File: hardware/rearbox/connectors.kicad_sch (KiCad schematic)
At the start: 2 parts, among them J3 Conn_02x28_Top_Bottom, J4 Auxiliary

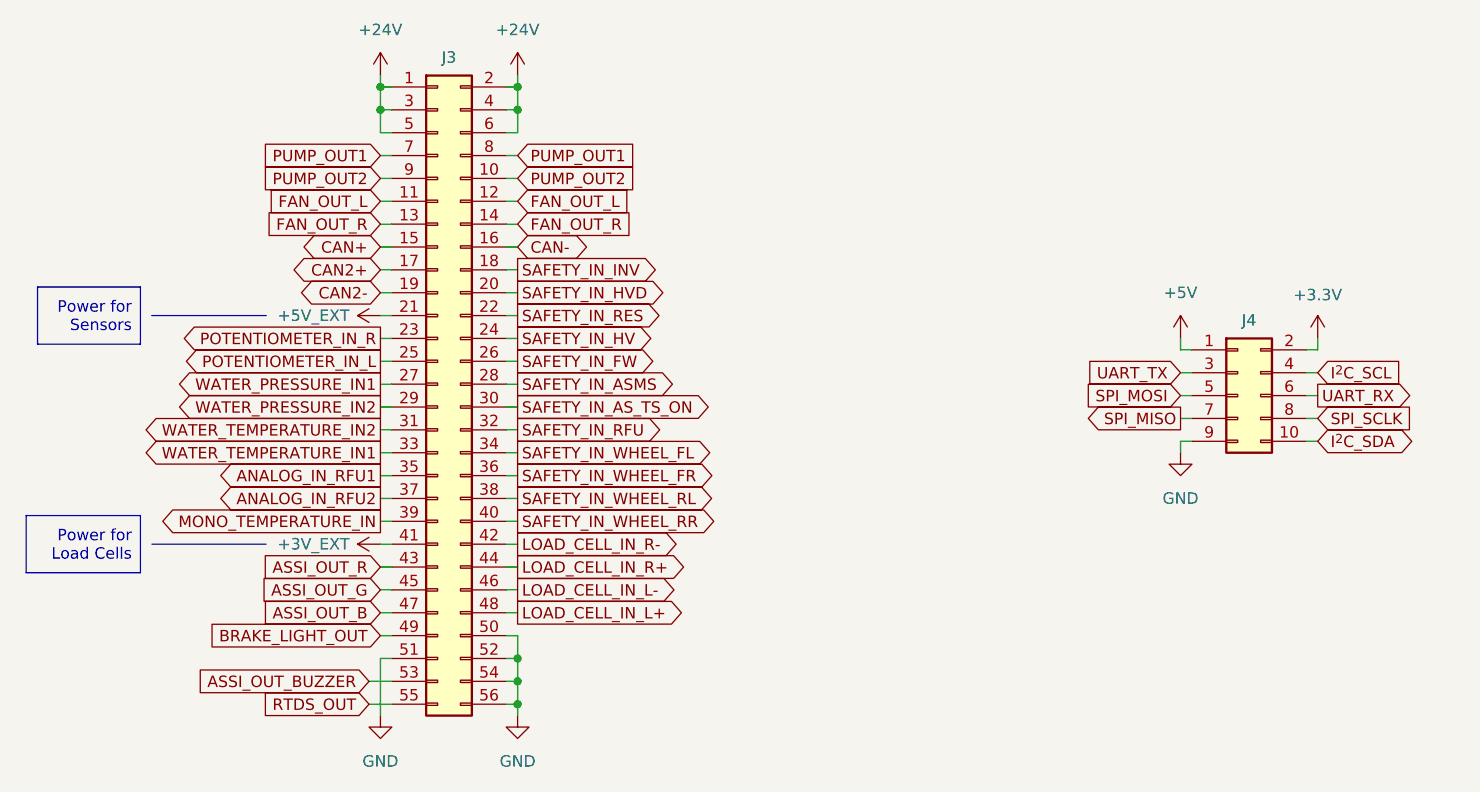
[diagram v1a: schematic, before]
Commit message: Deleted measurement systems for new iteration
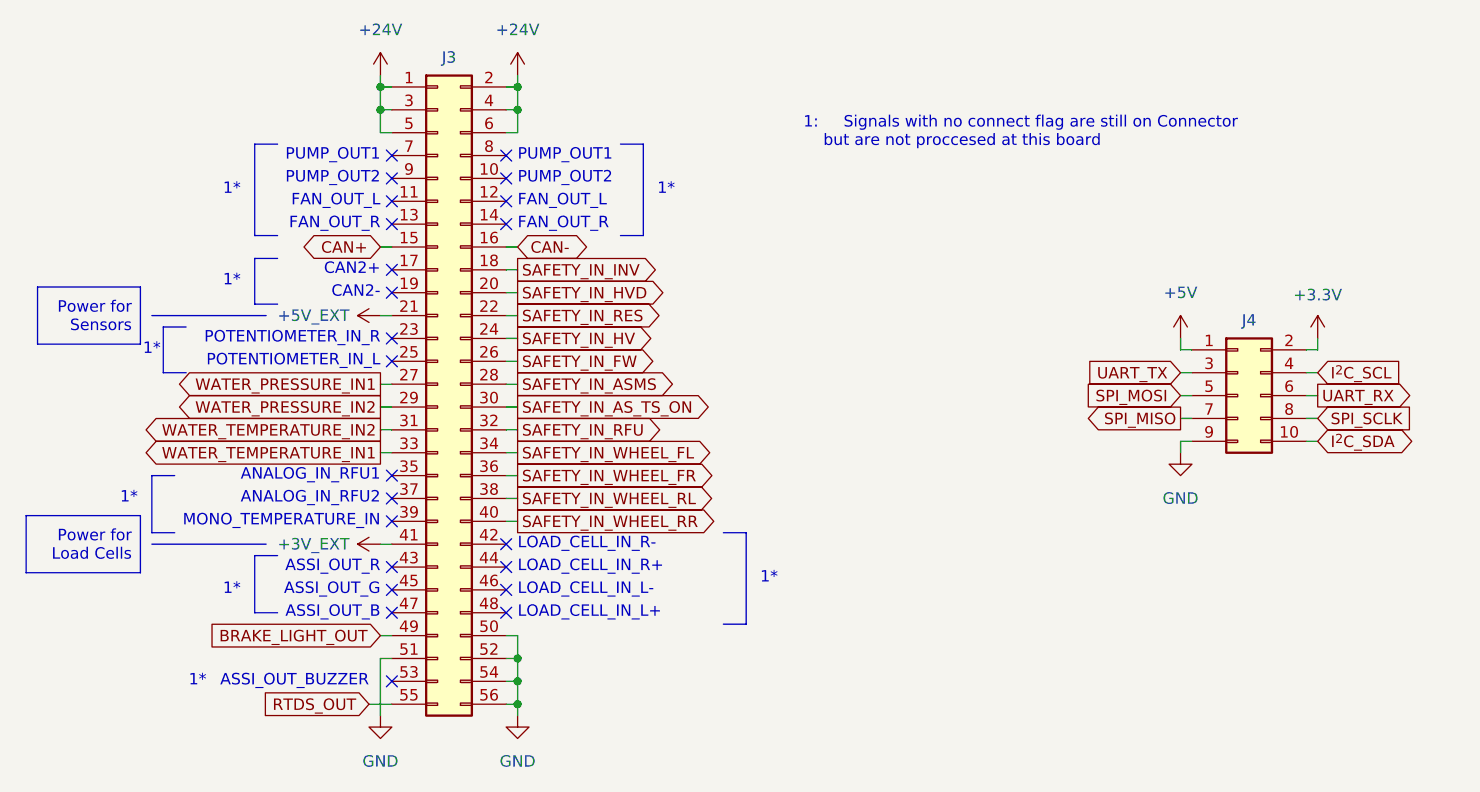
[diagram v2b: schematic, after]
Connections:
- net ANALOG_IN_RFU1: no longer names the net of J3.35 (Pin_35)
- net ANALOG_IN_RFU2: no longer names the net of J3.37 (Pin_37)
- net ASSI_OUT_B: no longer names the net of J3.47 (Pin_47)
- net ASSI_OUT_BUZZER: no longer names the net of J3.53 (Pin_53)
- net ASSI_OUT_G: no longer names the net of J3.45 (Pin_45)
- net ASSI_OUT_R: no longer names the net of J3.43 (Pin_43)
- net CAN2+: no longer names the net of J3.17 (Pin_17)
- net CAN2-: no longer names the net of J3.19 (Pin_19)
- net FAN_OUT_L: no longer names the net of J3.11 (Pin_11)
- net FAN_OUT_L: no longer J3.12 (Pin_12)
- net FAN_OUT_R: no longer names the net of J3.13 (Pin_13)
- net FAN_OUT_R: no longer J3.14 (Pin_14)
- net LOAD_CELL_IN_L+: no longer names the net of J3.48 (Pin_48)
- net LOAD_CELL_IN_L-: no longer names the net of J3.46 (Pin_46)
- net LOAD_CELL_IN_R+: no longer names the net of J3.44 (Pin_44)
- net LOAD_CELL_IN_R-: no longer names the net of J3.42 (Pin_42)
- net MONO_TEMPERATURE_IN: no longer names the net of J3.39 (Pin_39)
- net POTENTIOMETER_IN_L: no longer names the net of J3.25 (Pin_25)
- net POTENTIOMETER_IN_R: no longer names the net of J3.23 (Pin_23)
- net PUMP_OUT1: no longer names the net of J3.7 (Pin_7)
- net PUMP_OUT1: no longer J3.8 (Pin_8)
- net PUMP_OUT2: no longer names the net of J3.10 (Pin_10)
- net PUMP_OUT2: no longer J3.9 (Pin_9)
- no-connect marks 0 -> 23
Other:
- note added: "1*"
- note added: "1: Signals with no connect flag are still on Connector but are not proccesed at this board"
- note added: "ANALOG_IN_RFU1"
- note added: "ANALOG_IN_RFU2"
- note added: "ASSI_OUT_B"
- note added: "ASSI_OUT_BUZZER"
- note added: "ASSI_OUT_G"
- note added: "ASSI_OUT_R"
- note added: "CAN2+"
- note added: "CAN2-"
- note added: "FAN_OUT_L"
- note added: "FAN_OUT_R"
- note added: "LOAD_CELL_IN_L+"
- note added: "LOAD_CELL_IN_L-"
- note added: "LOAD_CELL_IN_R+"
- note added: "LOAD_CELL_IN_R-"
- note added: "MONO_TEMPERATURE_IN"
- note added: "POTENTIOMETER_IN_L"
- note added: "POTENTIOMETER_IN_R"
- note added: "PUMP_OUT1"
- note added: "PUMP_OUT2"

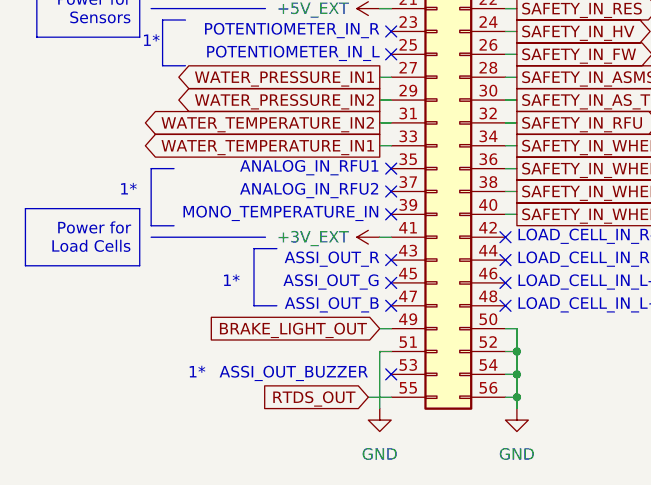
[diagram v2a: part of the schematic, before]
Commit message: Added an auxillary transistor for rear brakelights in case they burn up again and fixed some GNDISO_CAN problems
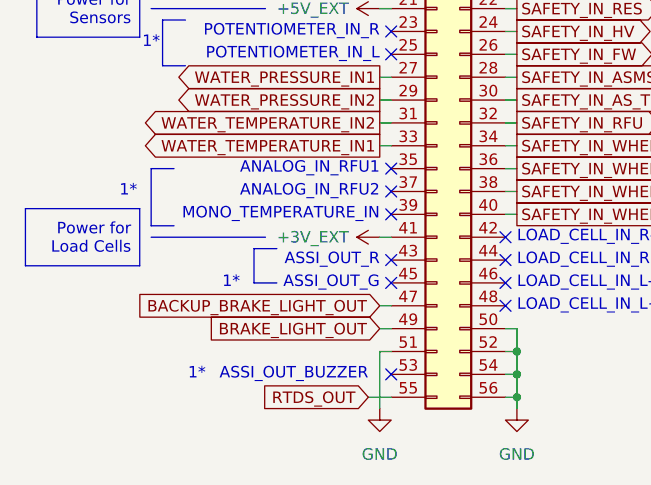
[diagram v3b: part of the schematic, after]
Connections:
- net BACKUP_BRAKE_LIGHT_OUT: now reaches J3.47 (Pin_47)
- no-connect marks 23 -> 22
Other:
- note removed: "ASSI_OUT_B"
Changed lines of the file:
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@@
-		)
-	)
-	(text "ASSI_OUT_B"
-		(exclude_from_sim no)
-		(at 106.68 124.46 0)
-		(effects
-			(font
-				(size 1.27 1.27)
-				(color 212 180 18 1)
-			)
-			(justify right)
 		)
 	)
@@
 	)
 	(no_connect
-		(at 107.95 124.46)
-	)
-	(no_connect
 		(at 120.65 73.66)
 	)
@@
 	(polyline
 		(pts
-			(xy 92.71 118.11) (xy 92.71 124.46)
+			(xy 92.71 118.11) (xy 92.71 121.92)
 		)
 		(stroke
@@
 	(polyline
 		(pts
-			(xy 92.71 124.46) (xy 95.25 124.46)
+			(xy 92.71 121.92) (xy 95.25 121.92)
 		)
 		(stroke
@@
 		(pts
 			(xy 195.58 102.87) (xy 196.85 102.87)
+		)
+		(stroke
+			(width 0)
+			(type default)
+		)
+	)
+	(wire
+		(pts
+			(xy 106.68 124.46) (xy 107.95 124.46)
 		)
 		(stroke
@@
 			(effects
 				(font
+					(size 1.27 1.27)
+				)
+				(justify right)
+				(hide yes)
+			)
+		)
+	)
+	(global_label "BACKUP_BRAKE_LIGHT_OUT"
+		(shape input)
+		(at 106.68 124.46 180)
+		(fields_autoplaced yes)
+		(effects
+			(font
+				(size 1.27 1.27)
+			)
+			(justify right)
+		)
+		(property "Intersheetrefs" "${INTERSHEET_REFS}"
+			(at 78.4157 124.46 0)
+			(effects
+				(font

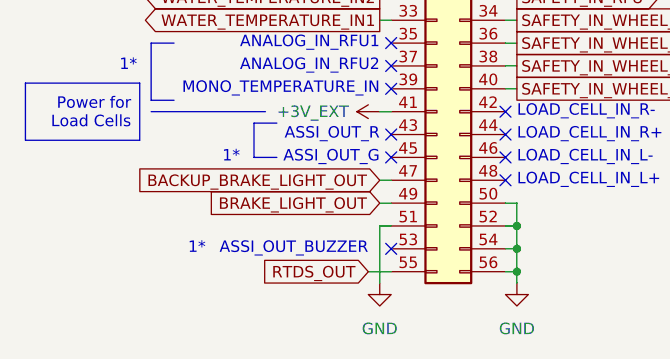
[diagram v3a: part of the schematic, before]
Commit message: Added an auxillary RTDS transistor as a backup
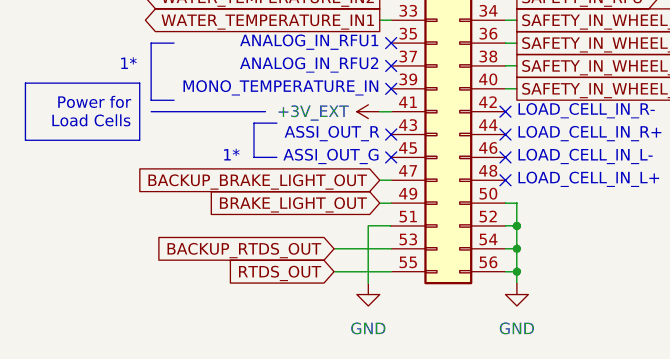
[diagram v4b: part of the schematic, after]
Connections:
- net BACKUP_RTDS_OUT: now reaches J3.53 (Pin_53)
- no-connect marks 22 -> 21
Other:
- note removed: "ASSI_OUT_BUZZER"
